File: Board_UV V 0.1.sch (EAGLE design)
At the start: 89 parts, among them IC1 74HC14D, IC4 74HC14D, IC5 MAX3232CSE, J2 POWER_JACK, Q1 500mA/300V, Q2 500mA/300V, U1 TLP521-4(GB), U2 TLP521-4(GB), U3 TLP521-4(GB), X1 22-23-2021, X2 1751303, X3 1751277, X4 22-23-2031, X5 22-23-2041, X6 1751280

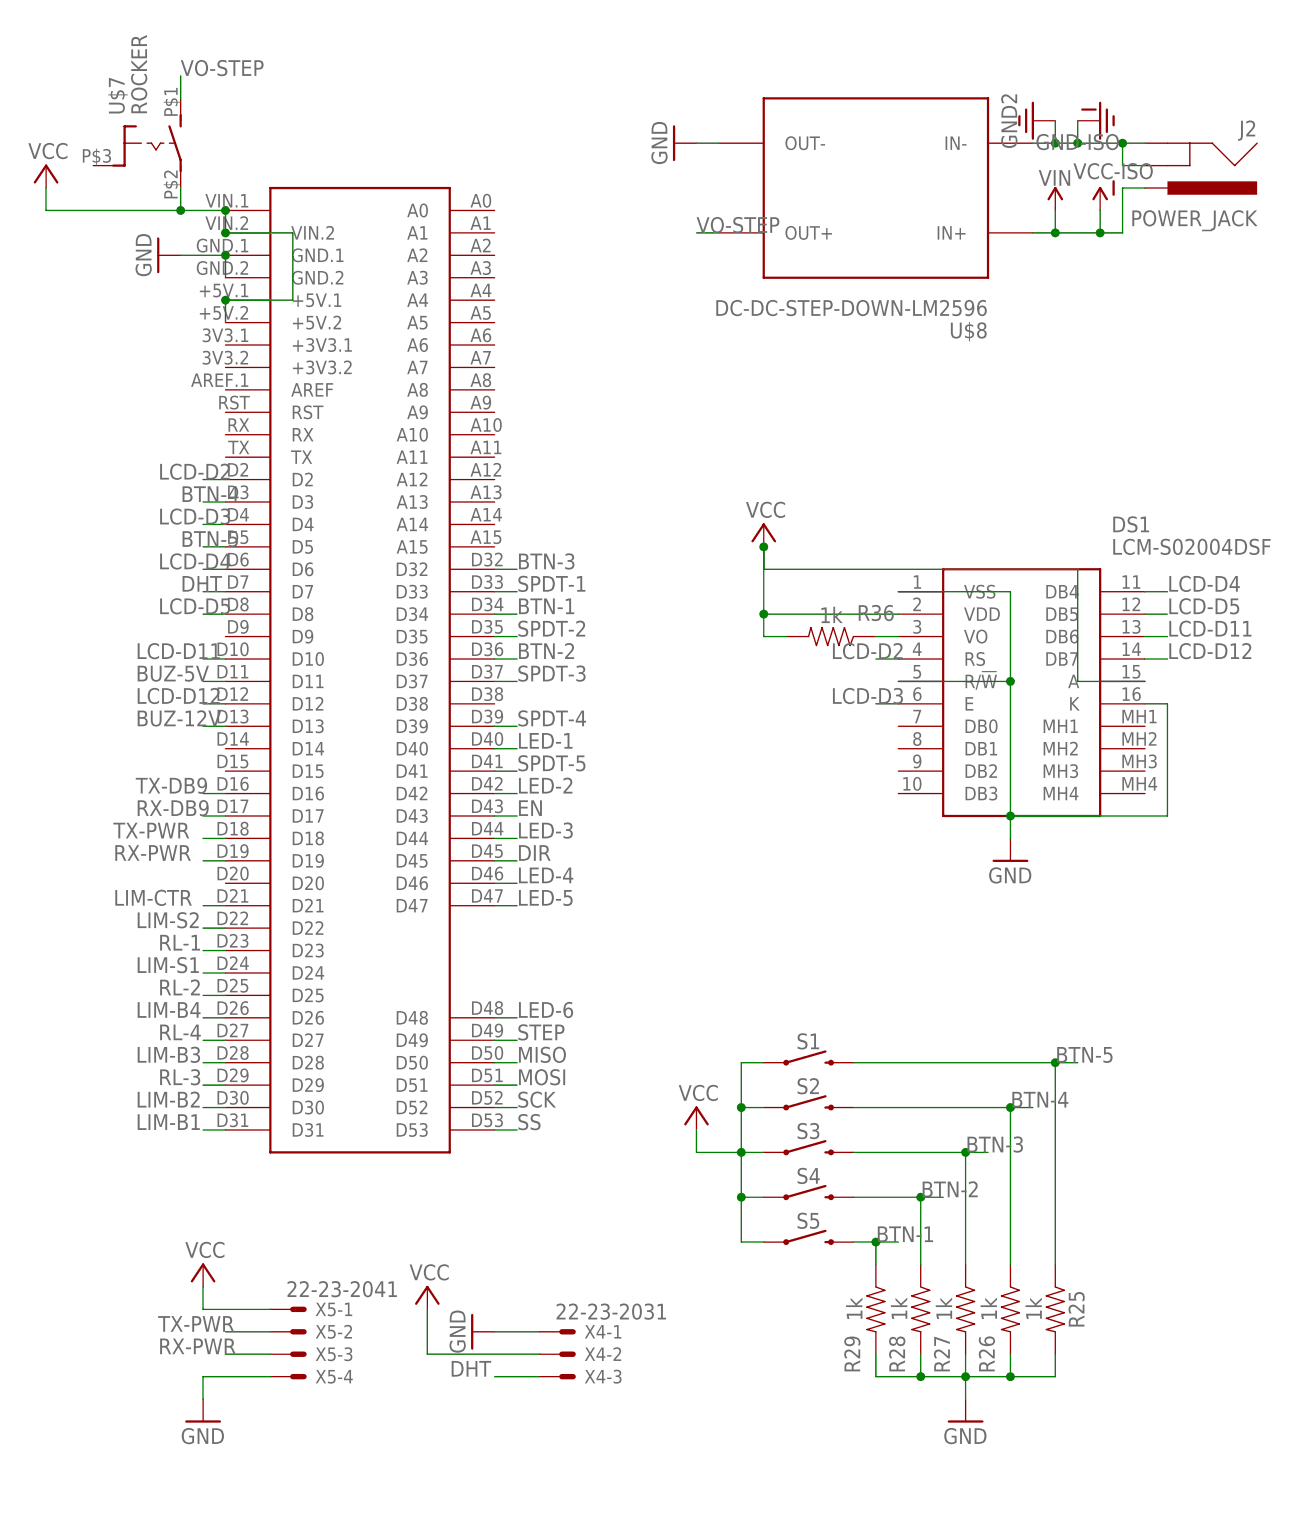
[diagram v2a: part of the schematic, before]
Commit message: change button power reset
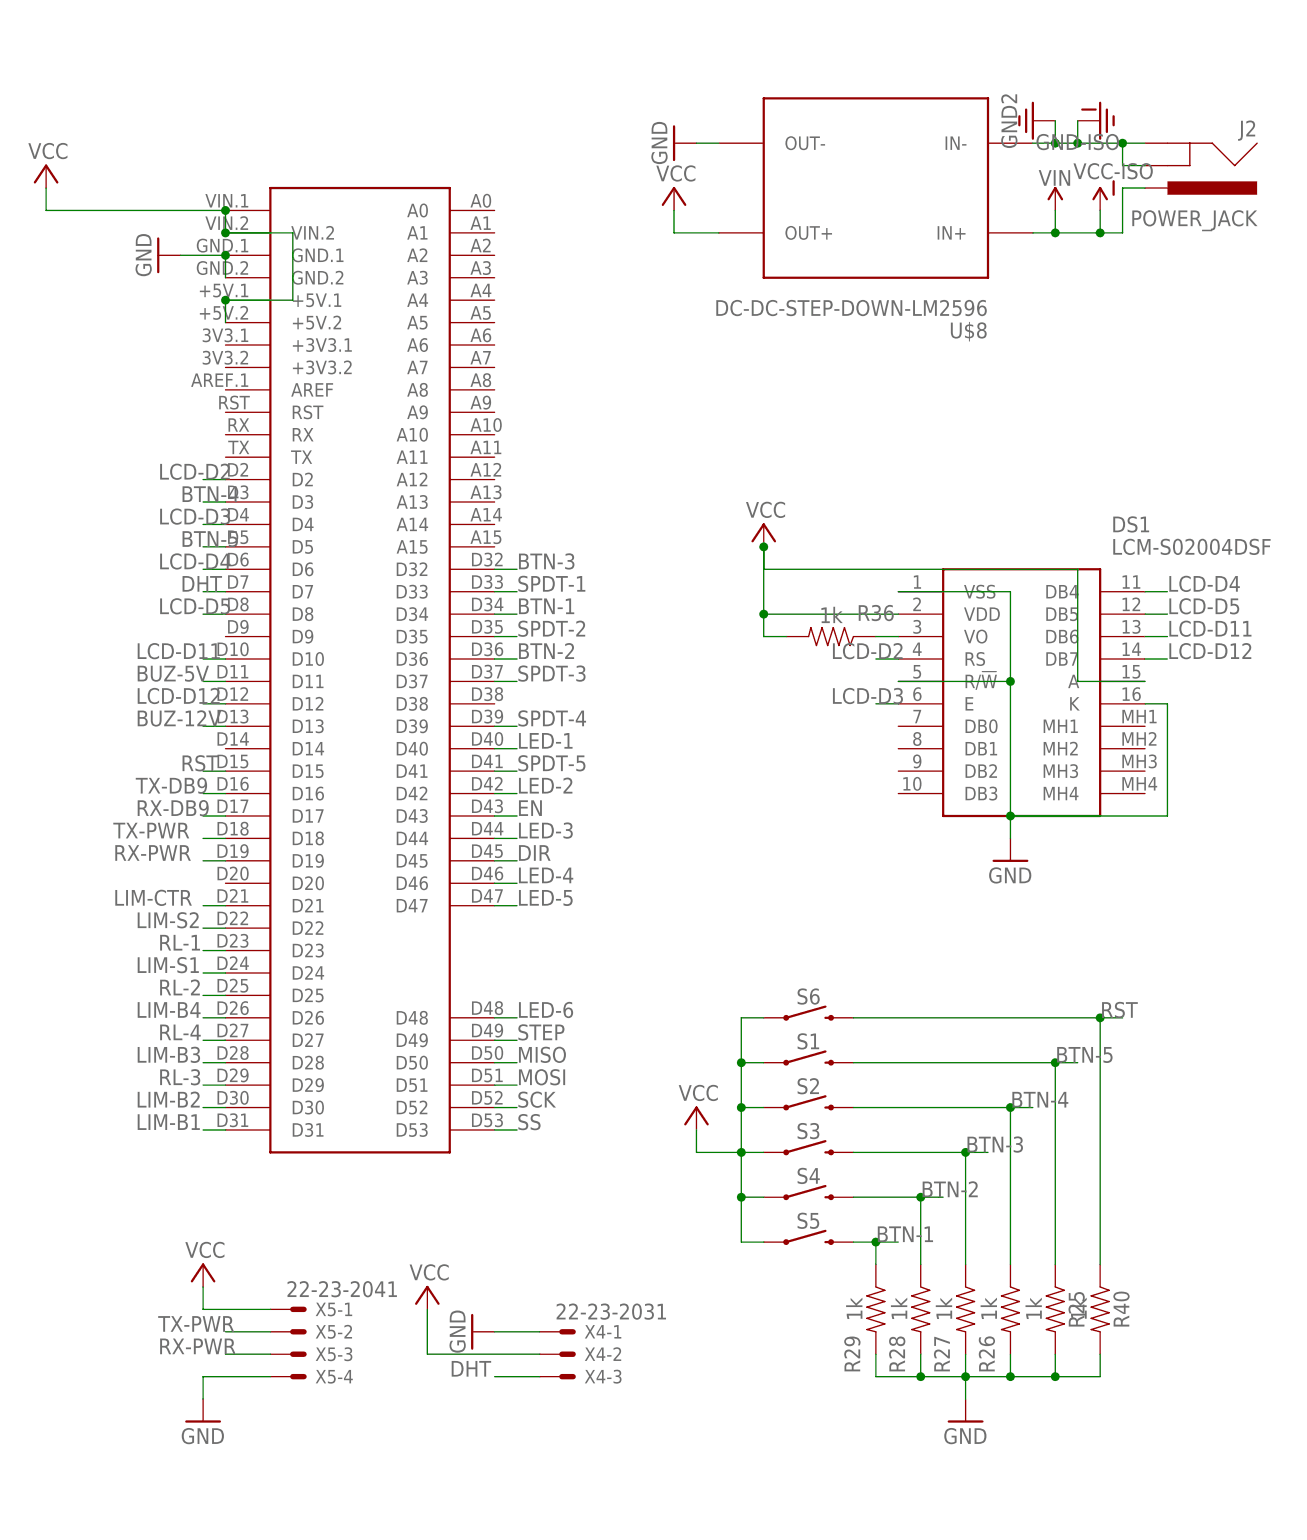
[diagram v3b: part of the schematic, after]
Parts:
- removed U$7: ROCKER, rocker sw:ROCKER
- added R40: 1k, SparkFun-Resistors:10KOHM-0603-1/10W-1%
- added S6: MOMENTARY-SWITCH-SPST-PTH-12MM, SparkFun-Switches:MOMENTARY-SWITCH-SPST-PTH-12MM
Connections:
- removed net VO-STEP: U$7.S, U$8.OUT+
- new net RST: R40.1, S6.2, U$1.D15
- net GND: now also R40.2
- net VCC: now also S6.1, U$8.OUT+; no longer U$7.P
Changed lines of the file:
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@@
 <part name="U$5" library="rocker sw" deviceset="ROCKER" device=""/>
 <part name="U$6" library="rocker sw" deviceset="ROCKER" device=""/>
-<part name="U$7" library="rocker sw" deviceset="ROCKER" device=""/>
 <part name="R37" library="SparkFun-Resistors" deviceset="10KOHM" device="-0603-1/10W-1%" value="1k"/>
 <part name="R38" library="SparkFun-Resistors" deviceset="10KOHM" device="-0603-1/10W-1%" value="1k"/>
@@
 <part name="U$12" library="SparkFun-PowerSymbols" deviceset="VCC-ISO" device=""/>
 <part name="GND-ISO10" library="SparkFun-PowerSymbols" deviceset="GND-ISO" device=""/>
+<part name="P+13" library="supply1" library_urn="urn:adsk.eagle:library:371" deviceset="VCC" device=""/>
+<part name="S6" library="SparkFun-Switches" deviceset="MOMENTARY-SWITCH-SPST" device="-PTH-12MM"/>
+<part name="R40" library="SparkFun-Resistors" deviceset="10KOHM" device="-0603-1/10W-1%" value="1k"/>
 </parts>
 <sheets>
@@
 <attribute name="VALUE" x="196.85" y="-60.325" size="1.778" layer="96" rot="R90"/>
 </instance>
-<instance part="U$7" gate="G$1" x="25.4" y="-53.34" smashed="yes">
-<attribute name="NAME" x="21.59" y="-50.165" size="1.778" layer="95" rot="R90"/>
-<attribute name="VALUE" x="24.13" y="-50.165" size="1.778" layer="96" rot="R90"/>
-</instance>
 <instance part="R37" gate="G$1" x="243.84" y="-71.12" smashed="yes">
 <attribute name="NAME" x="248.92" y="-74.676" size="1.778" layer="95" font="vector" align="bottom-center"/>
@@
 <instance part="GND-ISO10" gate="G$1" x="355.6" y="-154.94" smashed="yes">
 <attribute name="VALUE" x="352.298" y="-152.4" size="1.778" layer="96" rot="R90" align="top-center"/>
+</instance>
+<instance part="P+13" gate="VCC" x="83.82" y="-58.42" smashed="yes">
+<attribute name="VALUE" x="86.36" y="-55.88" size="1.778" layer="96" rot="R180"/>
+</instance>
+<instance part="S6" gate="G$1" x="99.06" y="-152.4" smashed="yes">
+<attribute name="NAME" x="99.06" y="-150.876" size="1.778" layer="95" font="vector" align="bottom-center"/>
+</instance>
+<instance part="R40" gate="G$1" x="132.08" y="-185.42" smashed="yes" rot="R270">
+<attribute name="NAME" x="133.604" y="-185.42" size="1.778" layer="95" font="vector" rot="R270" align="bottom-center"/>
+<attribute name="VALUE" x="130.556" y="-185.42" size="1.778" layer="96" font="vector" rot="R270" align="top-center"/>
 </instance>
 </instances>
@@
 <junction x="91.44" y="-162.56"/>
 <wire x1="86.36" y1="-167.64" x2="91.44" y2="-167.64" width="0.1524" layer="91"/>
+<pinref part="S6" gate="G$1" pin="1"/>
+<wire x1="93.98" y1="-152.4" x2="91.44" y2="-152.4" width="0.1524" layer="91"/>
+<wire x1="91.44" y1="-152.4" x2="91.44" y2="-157.48" width="0.1524" layer="91"/>
+<junction x="91.44" y="-157.48"/>
 </segment>
 <segment>
@@
 <wire x1="33.02" y1="-71.12" x2="33.02" y2="-73.66" width="0.1524" layer="91"/>
 <junction x="33.02" y="-71.12"/>
-<pinref part="U$7" gate="G$1" pin="P"/>
-<wire x1="27.94" y1="-58.42" x2="27.94" y2="-60.96" width="0.1524" layer="91"/>
-<wire x1="27.94" y1="-60.96" x2="33.02" y2="-60.96" width="0.1524" layer="91"/>
 <junction x="33.02" y="-60.96"/>
-<wire x1="12.7" y1="-60.96" x2="27.94" y2="-60.96" width="0.1524" layer="91"/>
-<junction x="27.94" y="-60.96"/>
+<wire x1="12.7" y1="-60.96" x2="33.02" y2="-60.96" width="0.1524" layer="91"/>
+</segment>
+<segment>
+<pinref part="P+13" gate="VCC" pin="VCC"/>
+<wire x1="83.82" y1="-60.96" x2="83.82" y2="-63.5" width="0.1524" layer="91"/>
+<pinref part="U$8" gate="G$1" pin="OUT+"/>
+<wire x1="83.82" y1="-63.5" x2="88.9" y2="-63.5" width="0.1524" layer="91"/>
 </segment>
 </net>
@@
 <pinref part="GND19" gate="1" pin="GND"/>
 <wire x1="116.84" y1="-195.58" x2="116.84" y2="-193.04" width="0.1524" layer="91"/>
+<pinref part="R40" gate="G$1" pin="2"/>
+<wire x1="132.08" y1="-190.5" x2="132.08" y2="-193.04" width="0.1524" layer="91"/>
+<wire x1="132.08" y1="-193.04" x2="127" y2="-193.04" width="0.1524" layer="91"/>
+<junction x="127" y="-193.04"/>
 </segment>
 <segment>
@@
 </segment>
 </net>
-<net name="VO-STEP" class="0">
-<segment>
-<pinref part="U$7" gate="G$1" pin="S"/>
-<wire x1="27.94" y1="-48.26" x2="27.94" y2="-45.72" width="0.1524" layer="91"/>
-<label x="27.94" y="-45.72" size="1.778" layer="95"/>
-</segment>
-<segment>
-<pinref part="U$8" gate="G$1" pin="OUT+"/>
-<wire x1="88.9" y1="-63.5" x2="86.36" y2="-63.5" width="0.1524" layer="91"/>
-<label x="86.36" y="-63.5" size="1.778" layer="95"/>
-</segment>
-</net>
 <net name="2A" class="0">
 <segment>
@@
 </segment>
 </net>
+<net name="RST" class="0">
+<segment>
+<pinref part="U$1" gate="G$1" pin="D15"/>
+<wire x1="33.02" y1="-124.46" x2="30.48" y2="-124.46" width="0.1524" layer="91"/>
+<label x="27.94" y="-124.46" size="1.778" layer="95"/>
+</segment>
+<segment>
+<pinref part="R40" gate="G$1" pin="1"/>
+<pinref part="S6" gate="G$1" pin="2"/>
+<wire x1="132.08" y1="-180.34" x2="132.08" y2="-152.4" width="0.1524" layer="91"/>
+<wire x1="132.08" y1="-152.4" x2="104.14" y2="-152.4" width="0.1524" layer="91"/>
+<wire x1="132.08" y1="-152.4" x2="134.62" y2="-152.4" width="0.1524" layer="91"/>
+<junction x="132.08" y="-152.4"/>
+<label x="132.08" y="-152.4" size="1.778" layer="95"/>
+</segment>
+</net>

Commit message: finalisasi and add name
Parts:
- removed J2: POWER_JACK, SparkFun-Connectors:POWER_JACK
- added X7: 1751248, con-phoenix-350:1751248
- renumbered S1 to BUTTON1, S2 to BUTTON2, S3 to BUTTON5, S4 to BUTTON4, S5 to BUTTON3, S6 to BUTTON6, U$2 to SWITCH5, U$3 to SWITCH1, U$4 to SWITCH2, U$5 to SWITCH3, U$6 to SWITCH4
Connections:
- net GND-ISO: now also X7-1.K; no longer J2.GND, J2.GNDBREAK
- net VCC-ISO: now also X7-2.K; no longer J2.PWR
